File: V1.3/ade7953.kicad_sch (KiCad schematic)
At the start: 57 parts, among them U2 ADE7953xCP, Y1 3.58MHz

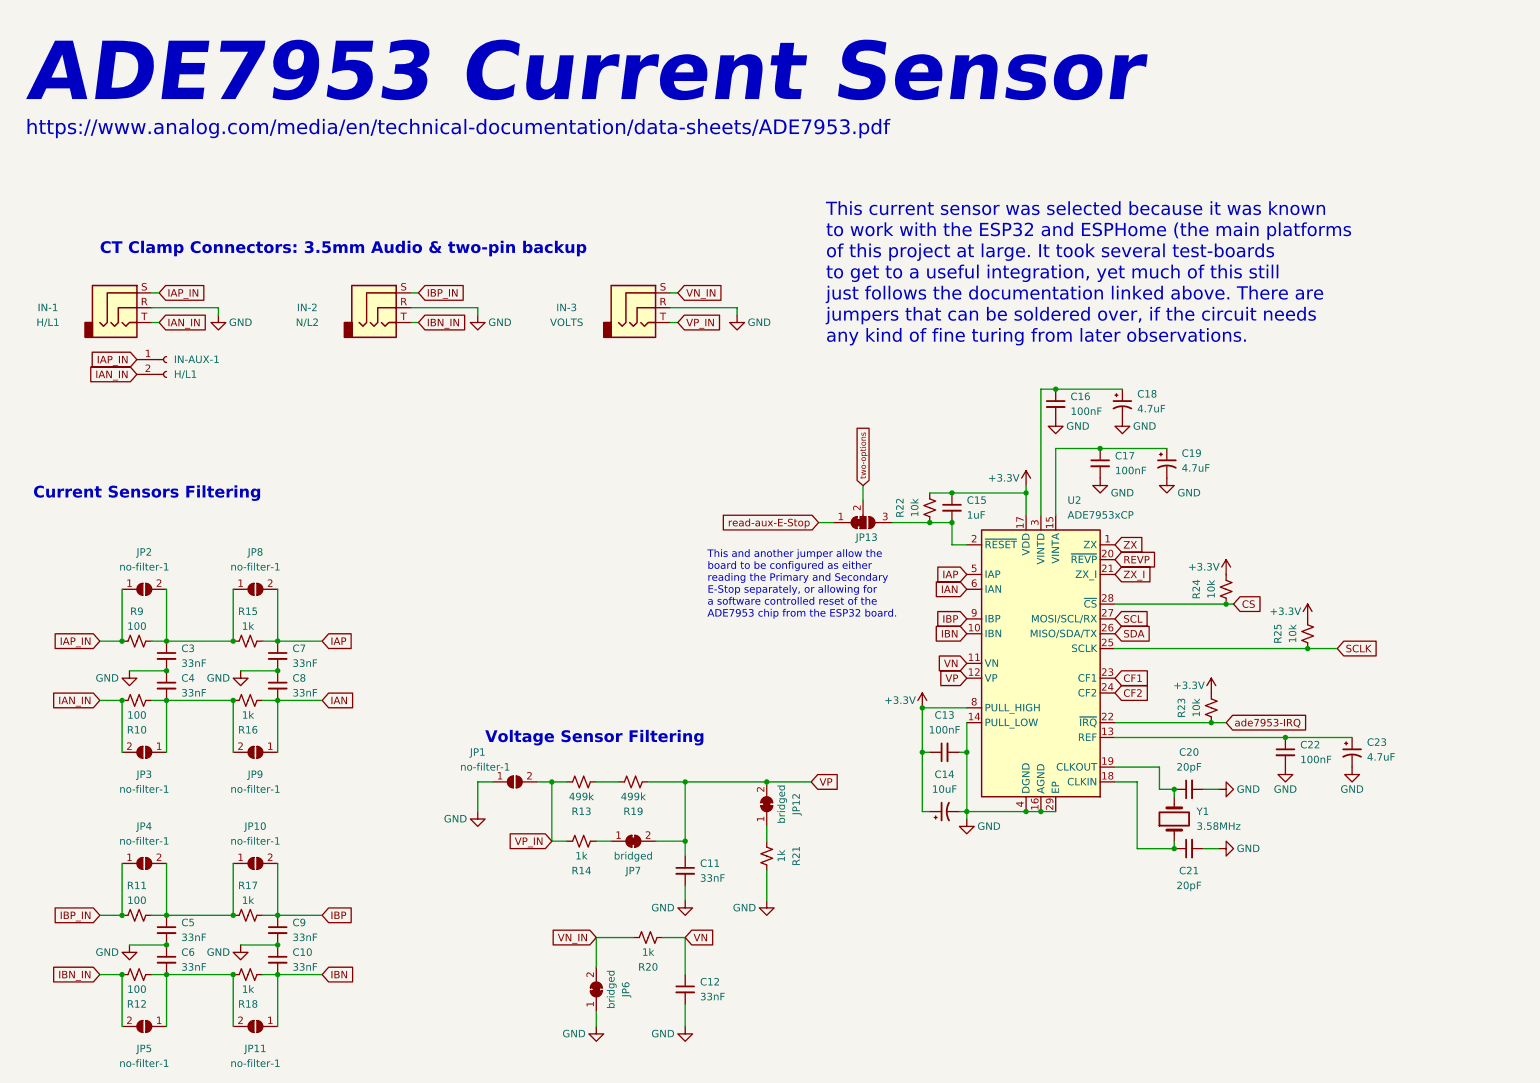
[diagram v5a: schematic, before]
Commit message: started adding the feather footprint to the board. need to update board shape and silkscreens
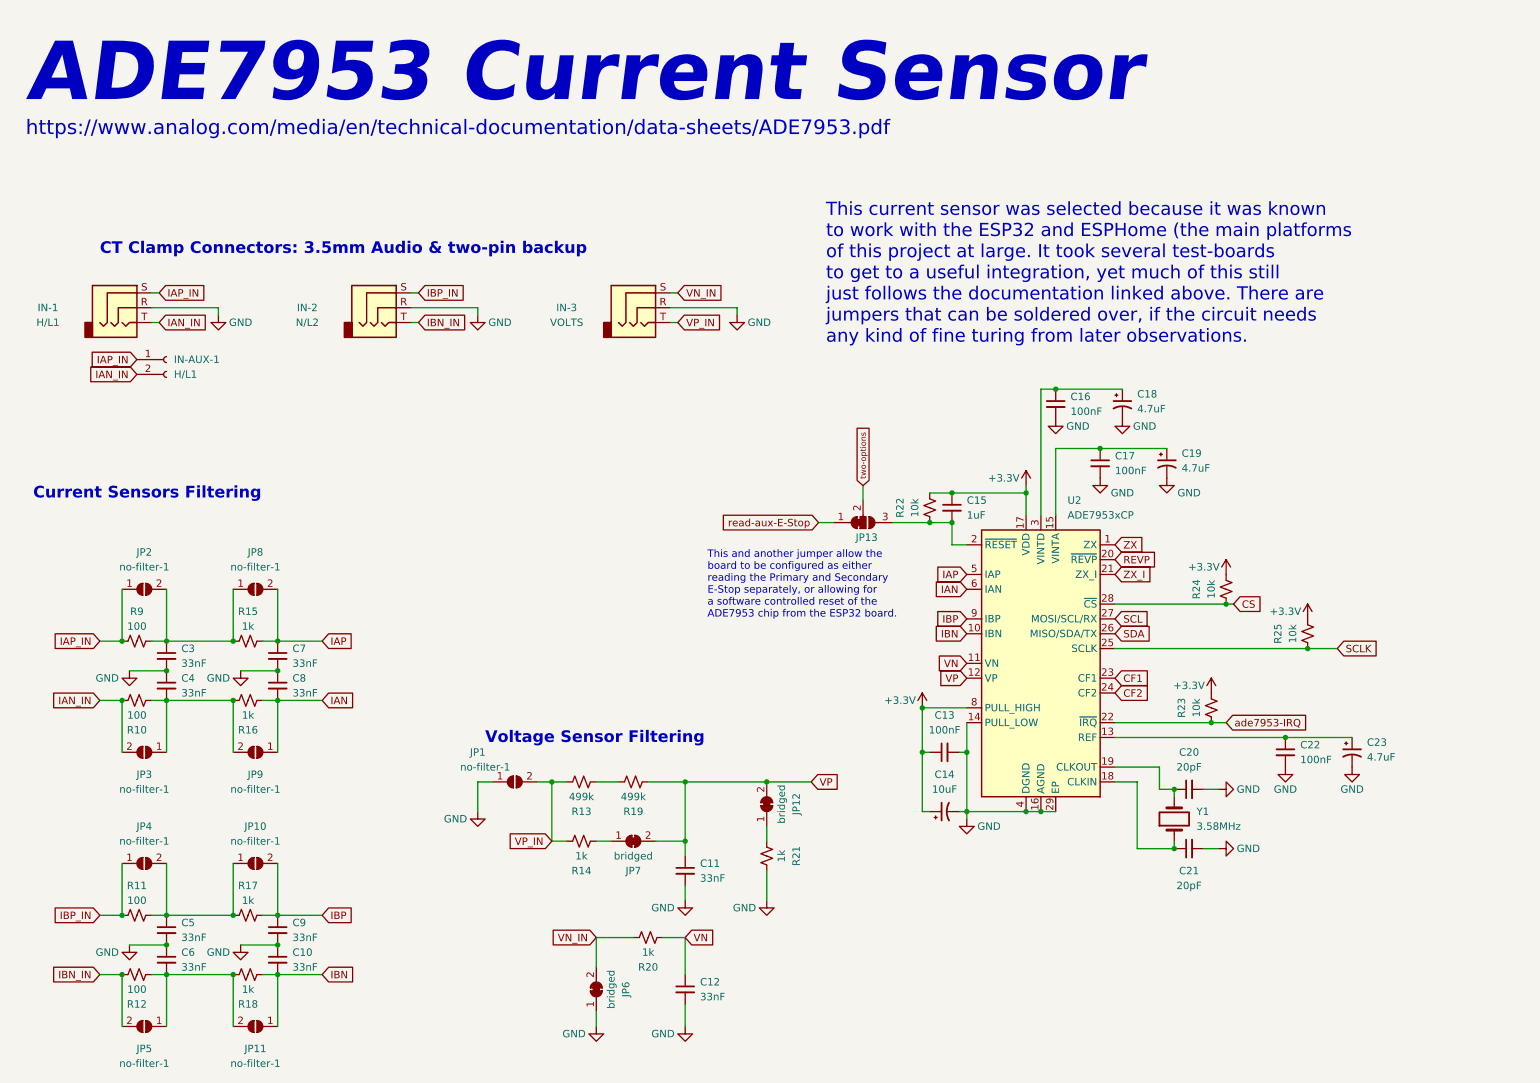
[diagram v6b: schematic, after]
